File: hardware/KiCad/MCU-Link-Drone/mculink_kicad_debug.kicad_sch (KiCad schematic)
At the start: 41 parts, among them J6 Conn_02x05_Odd_Even, U3 74LVC2T45DC, U4 SN74LVC1T45GW, U5 SN74LVC1T45GW, U6 MCP6001-OT, U7 SN74LVC1T45GW, U8 74LVC1G07

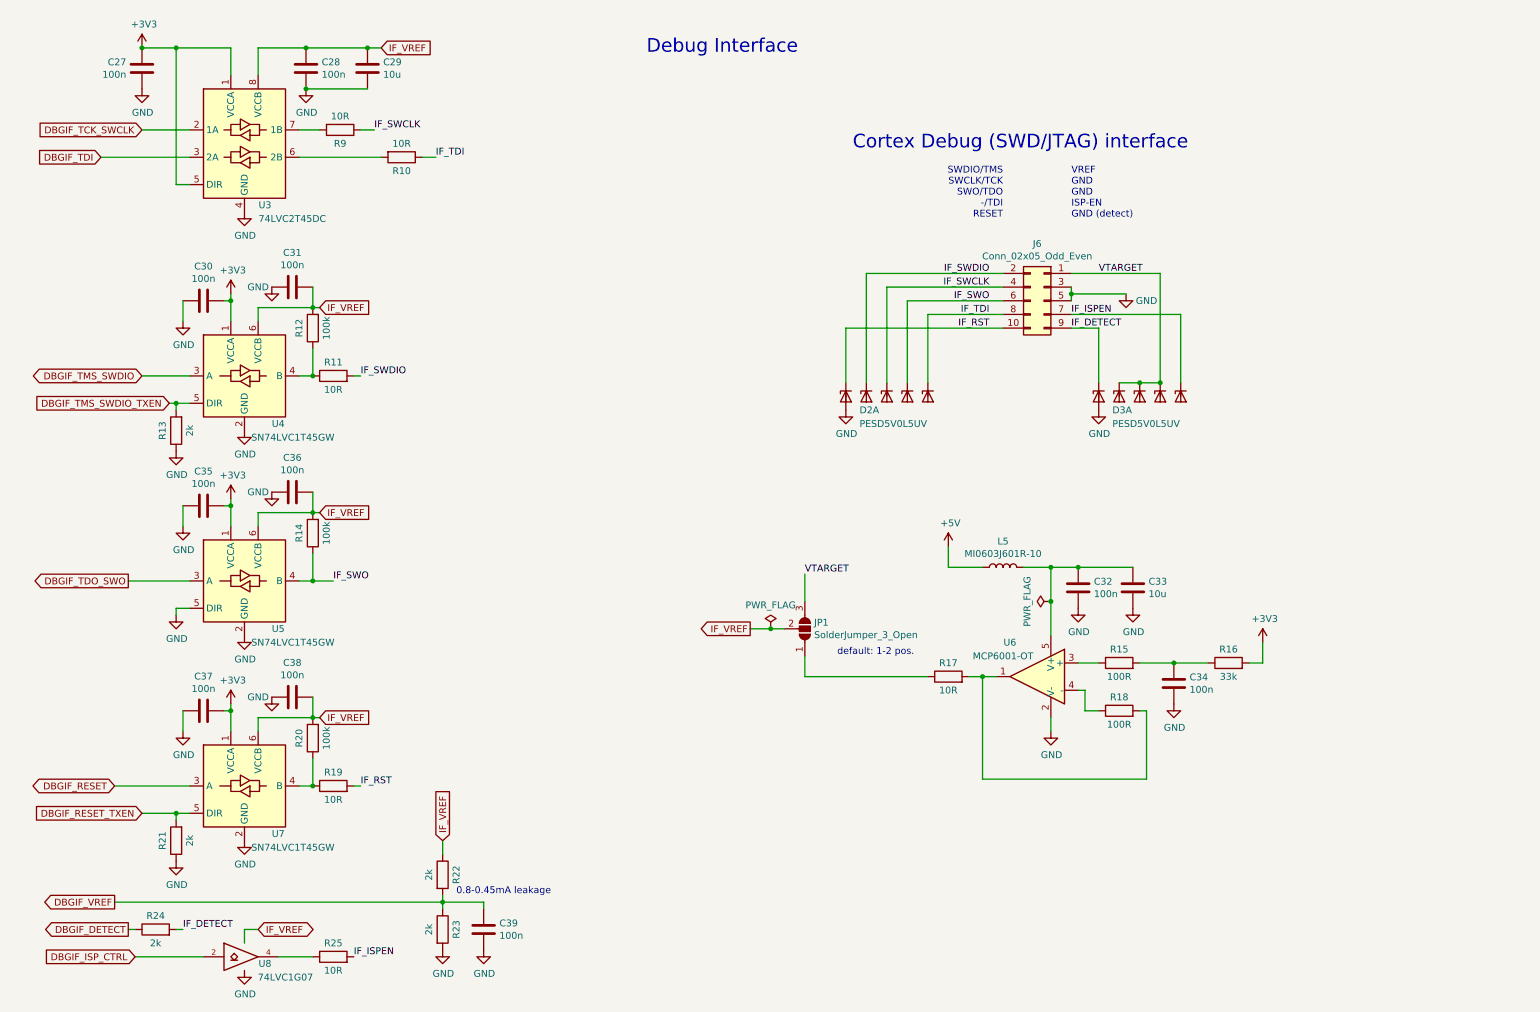
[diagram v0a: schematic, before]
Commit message: updated with drone project files
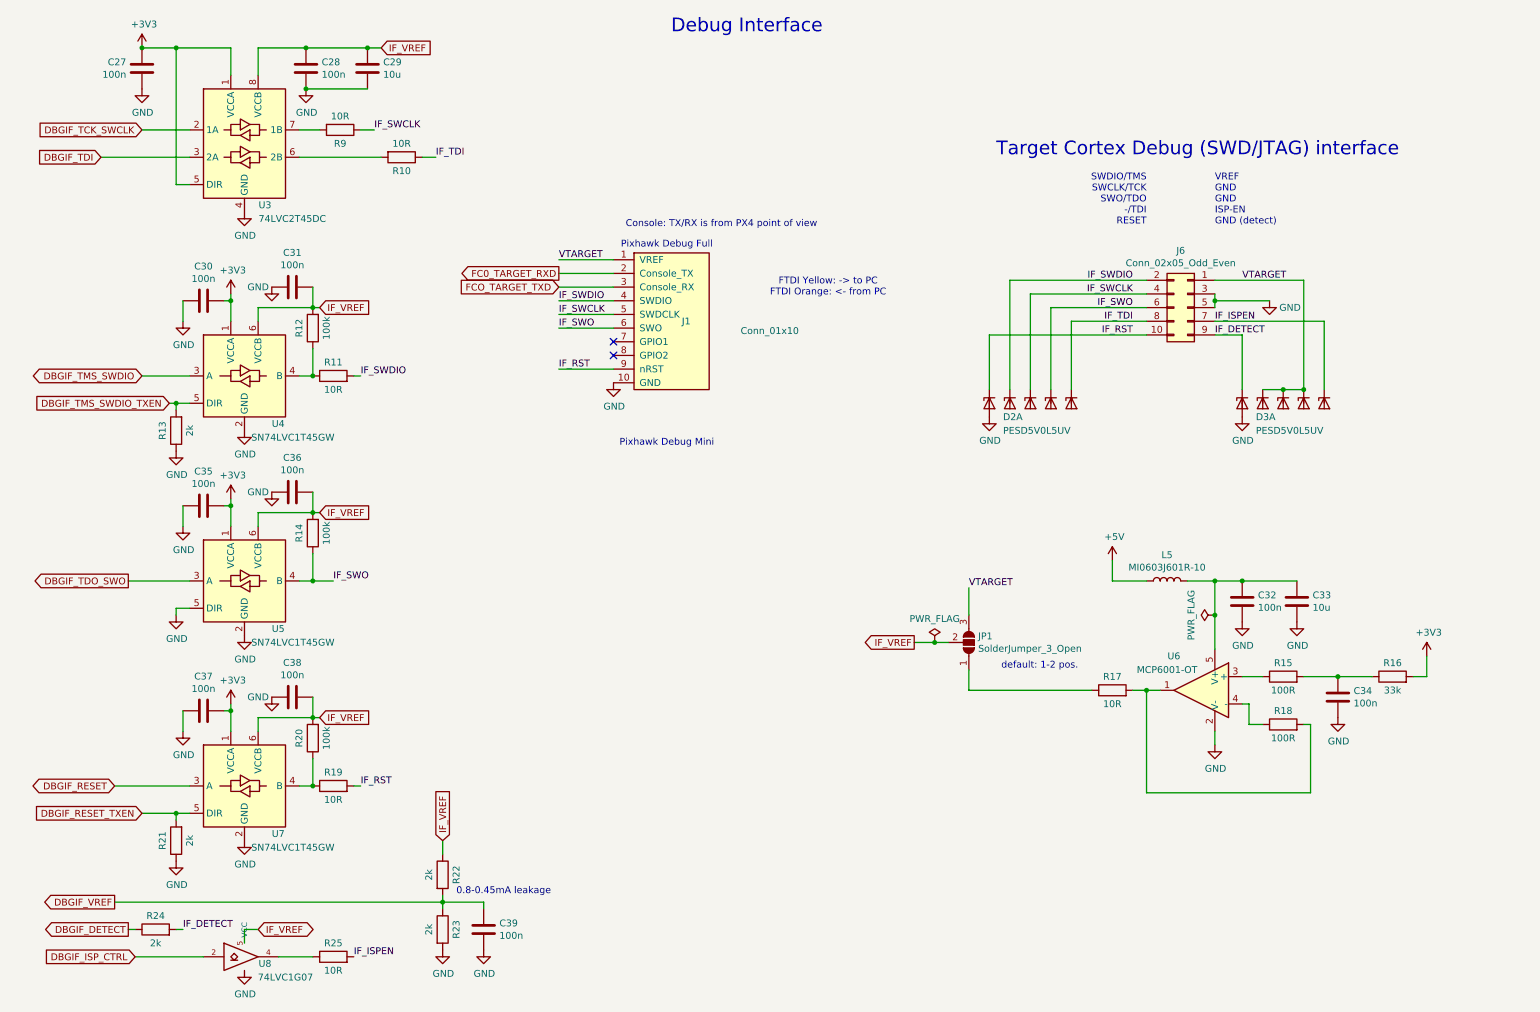
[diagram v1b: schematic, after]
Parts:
- added J1: Conn_01x10, Connector_JST:JST_SH_SM10B-SRSS-TB_1x10-1MP_P1.00mm_Horizontal, symbol McuOnEclipse:Pixhawk_Debug_Full
- U8: symbol mculink_kicad-rescue:74LVC1G07-74xGxx -> McuOnEclipse:74LVC1G07-74xGxx
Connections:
- net GND: now also J1.10 (GND)
- net IF_RST: now also J1.9 (nRST)
- net IF_SWCLK: now also J1.5 (SWDCLK)
- net IF_SWDIO: now also J1.4 (SWDIO)
- net IF_SWO: now also J1.6 (SWO)
- net VTARGET: now also J1.1 (VREF)
- net VCC renamed IF_VREF
- new net FC0_TARGET_RXD: J1.2 (Console_TX)
- new net FCO_TARGET_TXD: J1.3 (Console_RX)
- no-connect marks 0 -> 2
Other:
- note added: "Console: TX/RX is from PX4 point of view"
- note added: "FTDI Yellow: -> to PC FTDI Orange: <- from PC"
- note added: "Pixhawk Debug Full"
- note added: "Pixhawk Debug Mini"
- note added: "Target Cortex Debug (SWD/JTAG) interface"
- note removed: "Cortex Debug (SWD/JTAG) interface"
- moved on the sheet: C32, C33, C34, D2A, D3A, J6, JP1, L5, R15, R16, R17, R18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

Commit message: worked on layout
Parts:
- J6: footprint mculink_kicad:SWD_Pin_Header_Straight_2x05_Pitch1.27mm_SMD -> McuOnEclipse:SWD_Pin_Header_Straight_2x05_Pitch1.27mm_SMD_Shrouded
- U4, U5, U7: footprint Package_TO_SOT_SMD:SOT-23-6 -> Package_TO_SOT_SMD:SOT-363_SC-70-6
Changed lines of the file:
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@@
 			)
 		)
-		(property "Footprint" "Package_TO_SOT_SMD:SOT-23-6"
+		(property "Footprint" "Package_TO_SOT_SMD:SOT-363_SC-70-6"
 			(at 52.07 92.71 0)
 			(effects
@@
 			)
 		)
-		(property "Footprint" "mculink_kicad:SWD_Pin_Header_Straight_2x05_Pitch1.27mm_SMD"
+		(property "Footprint" "McuOnEclipse:SWD_Pin_Header_Straight_2x05_Pitch1.27mm_SMD_Shrouded"
 			(at 227.33 68.58 0)
 			(effects
@@
 			)
 		)
-		(property "Footprint" "Package_TO_SOT_SMD:SOT-23-6"
+		(property "Footprint" "Package_TO_SOT_SMD:SOT-363_SC-70-6"
 			(at 52.07 130.81 0)
 			(effects
@@
 			)
 		)
-		(property "Footprint" "Package_TO_SOT_SMD:SOT-23-6"
+		(property "Footprint" "Package_TO_SOT_SMD:SOT-363_SC-70-6"
 			(at 52.07 168.91 0)
 			(effects

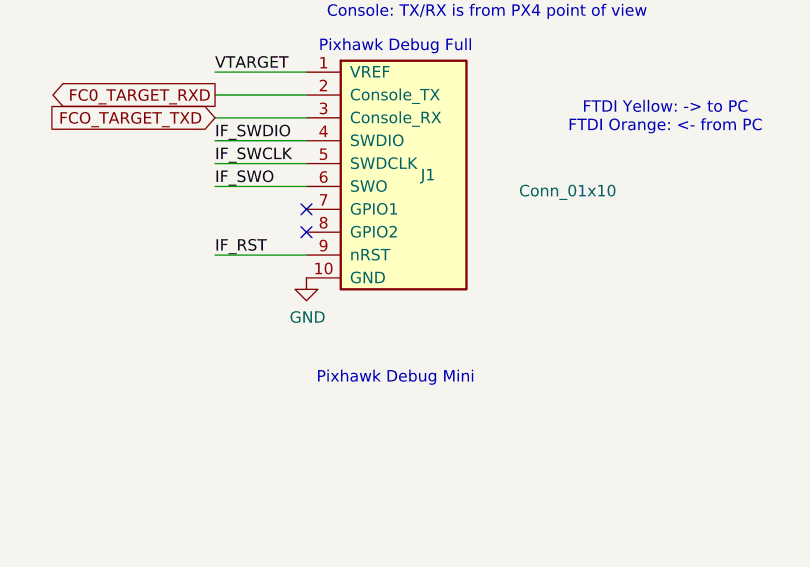
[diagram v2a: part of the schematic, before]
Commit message: fixed warnings
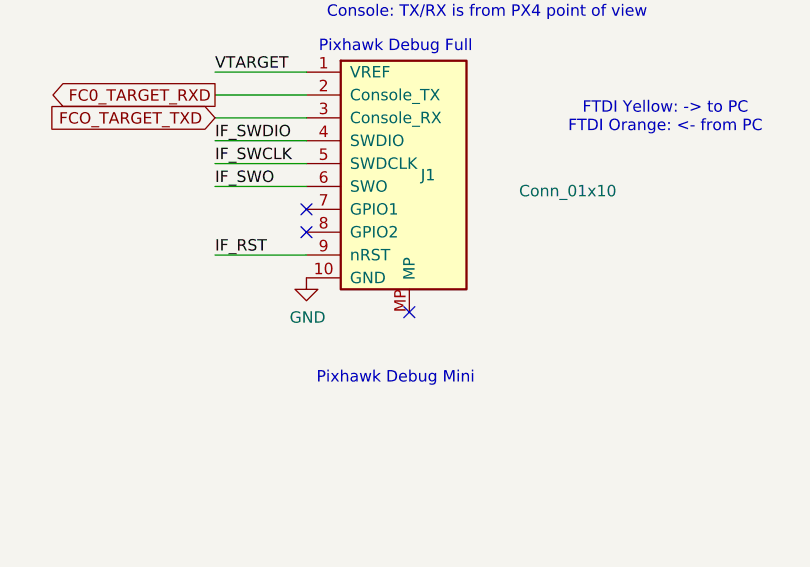
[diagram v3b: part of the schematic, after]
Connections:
- no-connect marks 2 -> 3

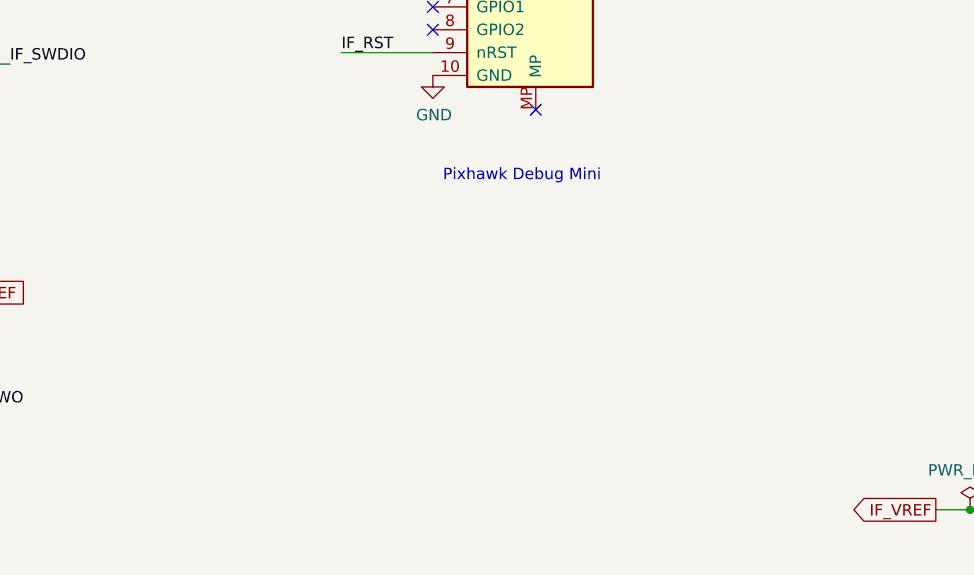
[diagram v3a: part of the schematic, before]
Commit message: added 3D models
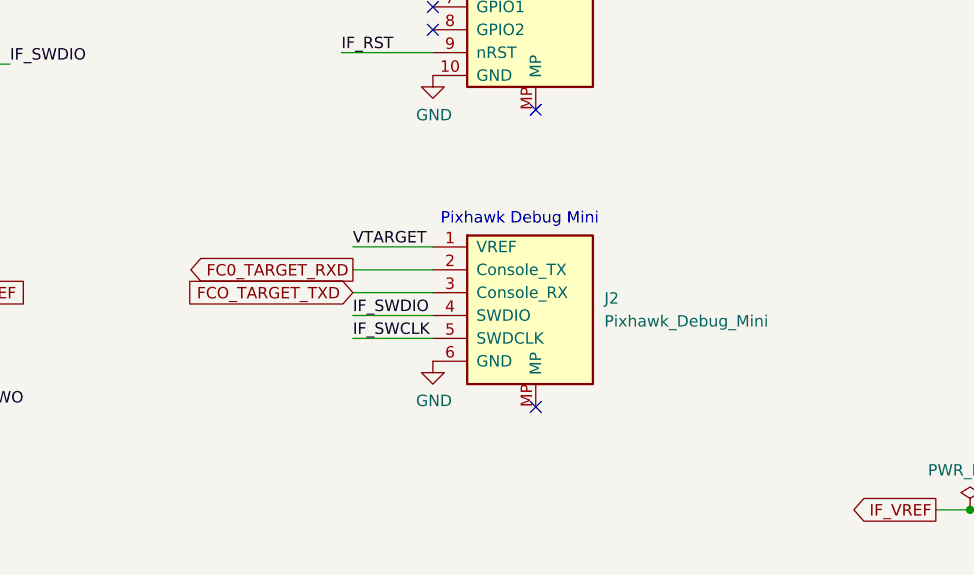
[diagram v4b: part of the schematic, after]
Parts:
- added J2: Pixhawk_Debug_Mini, McuOnEclipse:JST_SH_SM06B-SRSS-TB_1x06-1MP_P1.00mm_Horizontal, symbol McuOnEclipse:Pixhawk_Debug_Mini
- J1: footprint Connector_JST:JST_SH_SM10B-SRSS-TB_1x10-1MP_P1.00mm_Horizontal -> McuOnEclipse:JST_SH_SM10B-SRSS-TB_1x10-1MP_P1.00mm_Horizontal
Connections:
- net FC0_TARGET_RXD: now also J2.2 (Console_TX)
- net FCO_TARGET_TXD: now also J2.3 (Console_RX)
- net GND: now also J2.6 (GND)
- net IF_SWCLK: now also J2.5 (SWDCLK)
- net IF_SWDIO: now also J2.4 (SWDIO)
- net VTARGET: now also J2.1 (VREF)
- no-connect marks 3 -> 4

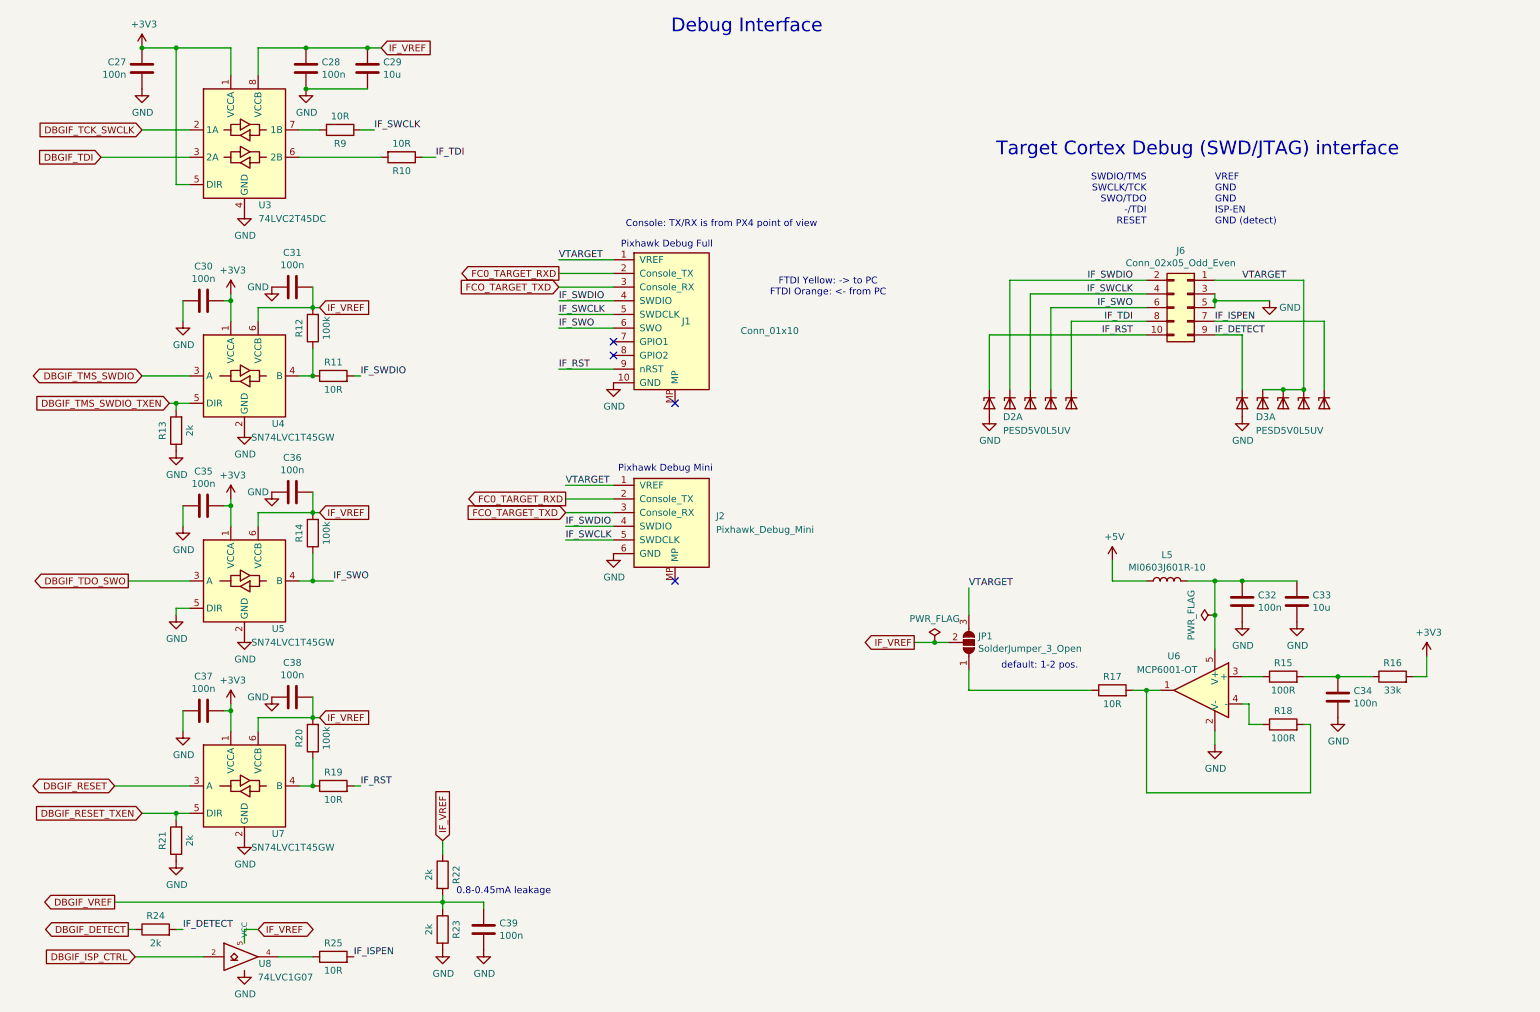
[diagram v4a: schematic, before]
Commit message: fixed warnings
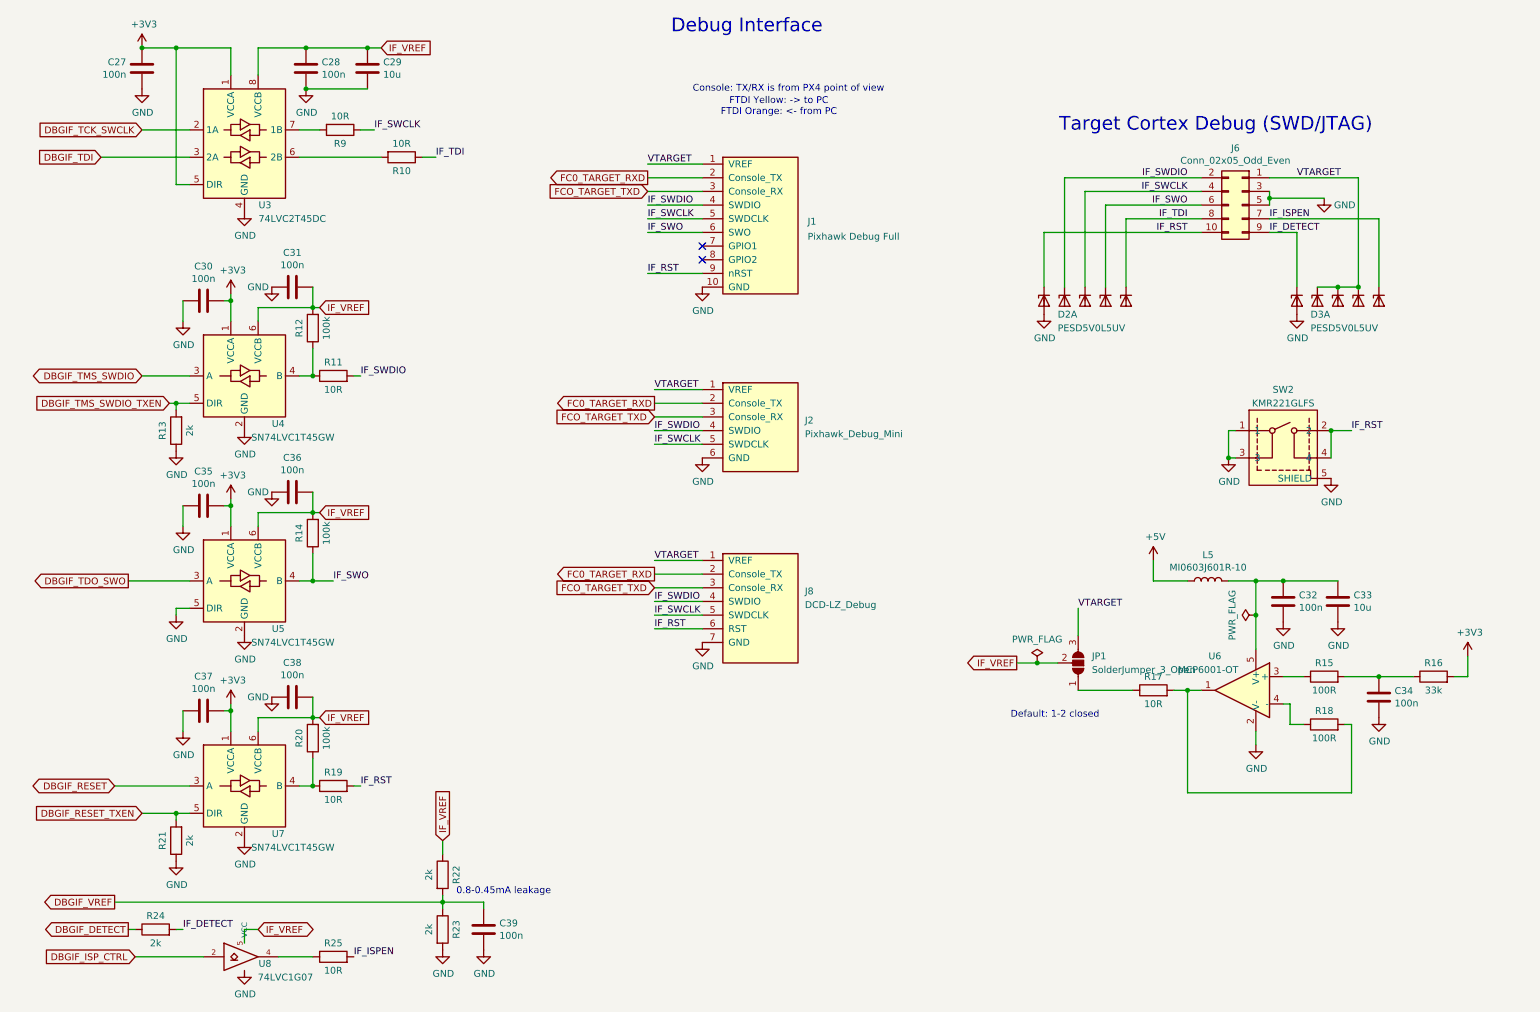
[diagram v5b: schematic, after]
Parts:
- removed JP1: SolderJumper_3_Open, Jumper:SolderJumper-3_P1.3mm_Open_RoundedPad1.0x1.5mm_NumberLabels, symbol mculink_kicad-rescue:SolderJumper_3_Open-Jumper
- added J8: DCD-LZ_Debug, McuOnEclipse:JST_GH_SM07B-GHS-TB_1x07-1MP_P1.25mm_Horizontal, symbol McuOnEclipse:DCD-LZ_Debug
- added JP1: SolderJumper_3_Open, McuOnEclipse:SolderJumper-3_P1.3mm_Open_RoundedPad1.0x1.5mm, symbol Jumper:SolderJumper_3_Open
- added SW2: KMR221GLFS, McuOnEclipse:SW_C_K_KMR2, symbol mculink_kicad:KMR221GLFS
- J1: value Conn_01x10 -> Pixhawk Debug Full
- J2: footprint McuOnEclipse:JST_SH_SM06B-SRSS-TB_1x06-1MP_P1.00mm_Horizontal -> McuOnEclipse:JST_SH_BM06B-SRSS-TB_1x06-1MP_P1.00mm_Vertical
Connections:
- net FC0_TARGET_RXD: now also J8.2 (Console_TX)
- net FCO_TARGET_TXD: now also J8.3 (Console_RX)
- net GND: now also J8.7 (GND), SW2.1, SW2.3, SW2.5 (SHIELD)
- net IF_RST: now also J8.6 (RST), SW2.2, SW2.4
- net IF_SWCLK: now also J8.5 (SWDCLK)
- net IF_SWDIO: now also J8.4 (SWDIO)
- net IF_VREF: now also JP1.2 (C)
- net VTARGET: now also J8.1 (VREF), JP1.3 (B)
- net at R17.1: now also JP1.1 (A)
- no-connect marks 4 -> 2
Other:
- note added: "Default: 1-2 closed"
- note added: "Target Cortex Debug (SWD/JTAG)"
- note removed: "Pixhawk Debug Full"
- note removed: "Pixhawk Debug Mini"
- note removed: "SWDIO/TMS SWCLK/TCK SWO/TDO -/TDI RESET"
- note removed: "Target Cortex Debug (SWD/JTAG) interface"
- note removed: "VREF GND GND ISP-EN GND (detect)"
- note removed: "default: 1-2 pos."
- moved on the sheet: C32, C33, C34, D2A, D3A, J6, L5, R15, R16, R17, R18, U6

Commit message: optimized layout
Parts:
- removed R25: 10R, Resistor_SMD:R_0603_1608Metric, symbol Device:R
- removed U8: 74LVC1G07, Package_TO_SOT_SMD:SOT-353_SC-70-5, symbol McuOnEclipse:74LVC1G07-74xGxx
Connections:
- net IF_SWDIO: now also D2.6 (K5); no longer D2.3 (K2)
- net IF_TDI: now also D2.3 (K2); no longer D2.6 (K5)
- net VTARGET: now also D3.6 (K5)
- net IF_ISPEN: no longer names the net of J6.7 (Pin_7)
- net IF_ISPEN: no longer D3.6 (K5)
- no-connect marks 2 -> 3

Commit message: optimized layout
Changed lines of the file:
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@@
 		(on_board yes)
 		(dnp no)
-		(fields_autoplaced yes)
 		(property "Reference" "JP1"
 			(at 209.55 133.3499 90)
@@
 		)
 		(property "Value" "SolderJumper_3_Open"
-			(at 209.55 135.8899 90)
+			(at 184.658 127.508 90)
 			(effects
 				(font
